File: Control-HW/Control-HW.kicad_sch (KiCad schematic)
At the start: 0 parts

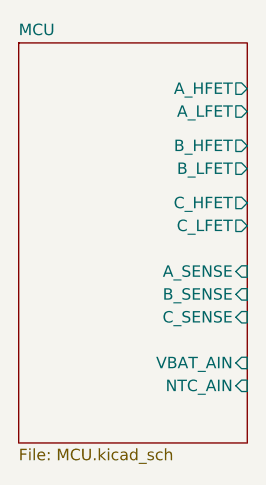
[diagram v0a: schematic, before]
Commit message: Assign pinout for MCU
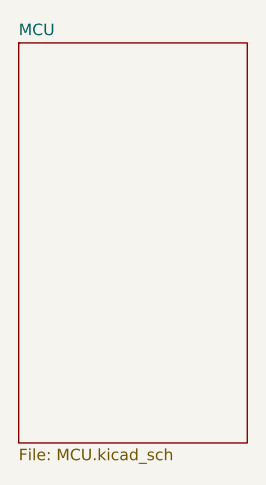
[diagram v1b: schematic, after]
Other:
- sheet MCU ports: added none; removed A_HFET, A_LFET, A_SENSE, B_HFET, B_LFET, B_SENSE, C_HFET, C_LFET, C_SENSE, NTC_AIN, VBAT_AIN
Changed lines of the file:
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@@
       (effects (font (size 1.27 1.27)) (justify left top))
-    )
-    (pin "VBAT_AIN" input (at 76.2 86.36 0)
-      (effects (font (size 1.27 1.27)) (justify right))
-    )
-    (pin "NTC_AIN" input (at 76.2 88.9 0)
-      (effects (font (size 1.27 1.27)) (justify right))
-    )
-    (pin "B_LFET" output (at 76.2 64.77 0)
-      (effects (font (size 1.27 1.27)) (justify right))
-    )
-    (pin "B_HFET" output (at 76.2 62.23 0)
-      (effects (font (size 1.27 1.27)) (justify right))
-    )
-    (pin "C_HFET" output (at 76.2 68.58 0)
-      (effects (font (size 1.27 1.27)) (justify right))
-    )
-    (pin "A_LFET" output (at 76.2 58.42 0)
-      (effects (font (size 1.27 1.27)) (justify right))
-    )
-    (pin "C_LFET" output (at 76.2 71.12 0)
-      (effects (font (size 1.27 1.27)) (justify right))
-    )
-    (pin "A_SENSE" input (at 76.2 76.2 0)
-      (effects (font (size 1.27 1.27)) (justify right))
-    )
-    (pin "B_SENSE" input (at 76.2 78.74 0)
-      (effects (font (size 1.27 1.27)) (justify right))
-    )
-    (pin "C_SENSE" input (at 76.2 81.28 0)
-      (effects (font (size 1.27 1.27)) (justify right))
-    )
-    (pin "A_HFET" output (at 76.2 55.88 0)
-      (effects (font (size 1.27 1.27)) (justify right))
     )
   )
@@
   )
   (symbol_instances
+    (path "/0efb9293-af2b-4951-be8b-c2bbb9c050db/00973212-ec5e-42aa-a37a-79f27234f35b"
+      (reference "#PWR?") (unit 1) (value "GND") (footprint "")
+    )
+    (path "/0efb9293-af2b-4951-be8b-c2bbb9c050db/11e08c2d-72e4-4ebc-84f9-78de55bff75f"
+      (reference "#PWR?") (unit 1) (value "+5V") (footprint "")
+    )
     (path "/0efb9293-af2b-4951-be8b-c2bbb9c050db/2790ea62-b87c-4368-91dd-07cfef8fd569"
       (reference "#PWR?") (unit 1) (value "+5V") (footprint "")
@@
     )
     (path "/0efb9293-af2b-4951-be8b-c2bbb9c050db/61b49617-a56e-4de8-b216-6e03e4cc29b6"
+      (reference "#PWR?") (unit 1) (value "+5V") (footprint "")
+    )
+    (path "/0efb9293-af2b-4951-be8b-c2bbb9c050db/704531c6-2635-453c-b25e-9f882da075da"
+      (reference "#PWR?") (unit 1) (value "GND") (footprint "")
+    )
+    (path "/0efb9293-af2b-4951-be8b-c2bbb9c050db/7c5093d5-c4e4-424a-9882-ca06fa196320"
       (reference "#PWR?") (unit 1) (value "+5V") (footprint "")
     )
@@
       (reference "C?") (unit 1) (value "100n") (footprint "C_Capacitor:C_0603")
     )
+    (path "/0efb9293-af2b-4951-be8b-c2bbb9c050db/8a25ffb8-c656-4c3a-9e11-2b8b4225422c"
+      (reference "C?") (unit 1) (value "100n") (footprint "C_Capacitor:C_0603")
+    )
     (path "/0efb9293-af2b-4951-be8b-c2bbb9c050db/8c6402f6-d1cd-48f0-83e7-512278a420e6"
       (reference "C?") (unit 1) (value "100n") (footprint "C_Capacitor:C_0603")
@@
       (reference "C?") (unit 1) (value "100n") (footprint "C_Capacitor:C_0603")
     )
+    (path "/0efb9293-af2b-4951-be8b-c2bbb9c050db/1895b57a-ad64-4af4-bdb7-7be6ec5fc16b"
+      (reference "N?") (unit 1) (value "TC2030_NL_SWD") (footprint "N_NonPart:TagConnect_2030_NL")
+    )
+    (path "/0efb9293-af2b-4951-be8b-c2bbb9c050db/a97c3e36-9e3f-4703-8a3f-97a45d71789d"
+      (reference "R?") (unit 1) (value "10K") (footprint "R_Resistor:R_0603")
+    )
+    (path "/0efb9293-af2b-4951-be8b-c2bbb9c050db/a9d4eee4-332e-4ba9-a13e-27840721190c"
+      (reference "R?") (unit 1) (value "10K") (footprint "R_Resistor:R_0603")
+    )
     (path "/0efb9293-af2b-4951-be8b-c2bbb9c050db/d2c77160-ff94-4c27-8994-8ee0fbce11da"

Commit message: First pass at control HW
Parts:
- added J?: Pins_2.54_1x12, J_Connector:Pins-2.54-1x12, symbol J_Connector:Pins_2.54_1x12
- added N? (x5): Pad_4x2, N_NonPart:Pad_4x2, symbol N_NonPart:Pad_4x2
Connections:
- new net +5V: N?.1
- new net Drivers/GATE_AH: J?.2
- new net Drivers/GATE_AL: J?.3
- new net Drivers/GATE_BH: J?.5
- new net Drivers/GATE_BL: J?.6
- new net Drivers/GATE_CH: J?.8
- new net Drivers/GATE_CL: J?.9
- new net Drivers/PHASE_A: J?.4
- new net Drivers/PHASE_B: J?.7
- new net Drivers/PHASE_C: J?.10
- new net GND: J?.1, J?.11, N?.1, N?.1
- new net MCU/RC_IN: N?.1
- new net MCU/VBATT: J?.12
- new net Power/BATT_2S: N?.1
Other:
- added sheet Drivers (Drivers.kicad_sch)
- added sheet Power (power.kicad_sch)
- added sheet Sense (Sense.kicad_sch)
- sheet MCU ports: added PWM_AH, PWM_AL, PWM_BH, PWM_BL, PWM_CH, PWM_CL, RC_IN, SENSE_A, SENSE_B, SENSE_C, SENSE_COM, VBATT; removed none
- note added: "BATT_2S"
- note added: "RADIO"

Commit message: First revision
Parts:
- gave numbers to parts that had none: 6
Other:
- note added: "To PCB: FET-HW"
- moved on the sheet: J1, N1, N2, N3, N4, N5

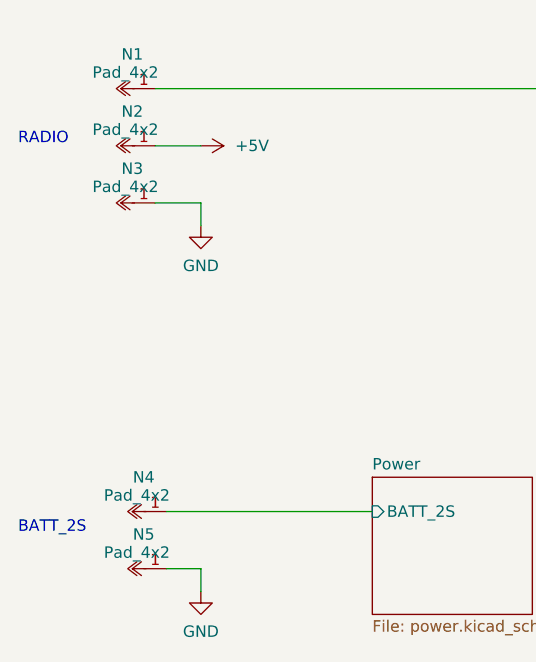
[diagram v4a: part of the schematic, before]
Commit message: Implemented control pcb
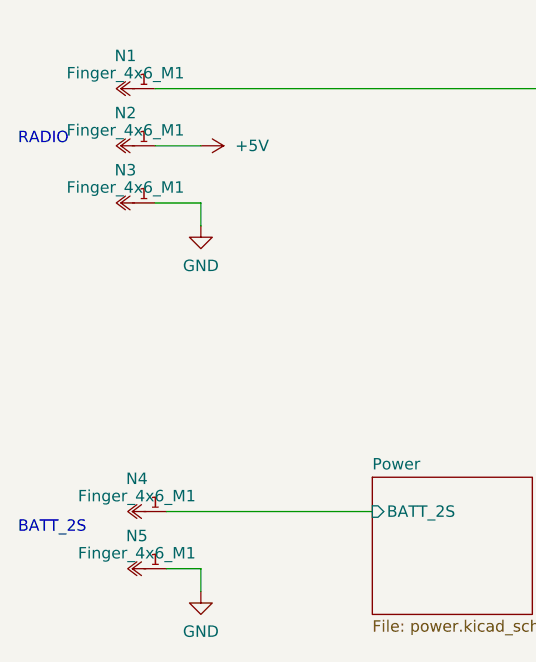
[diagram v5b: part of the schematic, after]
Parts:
- removed N1, N2, N3, N4, N5: Pad_4x2, N_NonPart:Pad_4x2, symbol N_NonPart:Pad_4x2
- added N1, N2, N3, N4, N5: Finger_4x6_M1, N_NonPart:Finger_4x6_M1, symbol N_NonPart:Finger_4x6_M1
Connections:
- net +5V: now also N2.1
- net GND: now also N3.1, N5.1
- net MCU/RC_IN: now also N1.1
- net Power/BATT_2S: now also N4.1
